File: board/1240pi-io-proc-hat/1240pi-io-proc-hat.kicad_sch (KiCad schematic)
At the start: 6 parts, among them J21 Header, P445 Header, U445 Z80

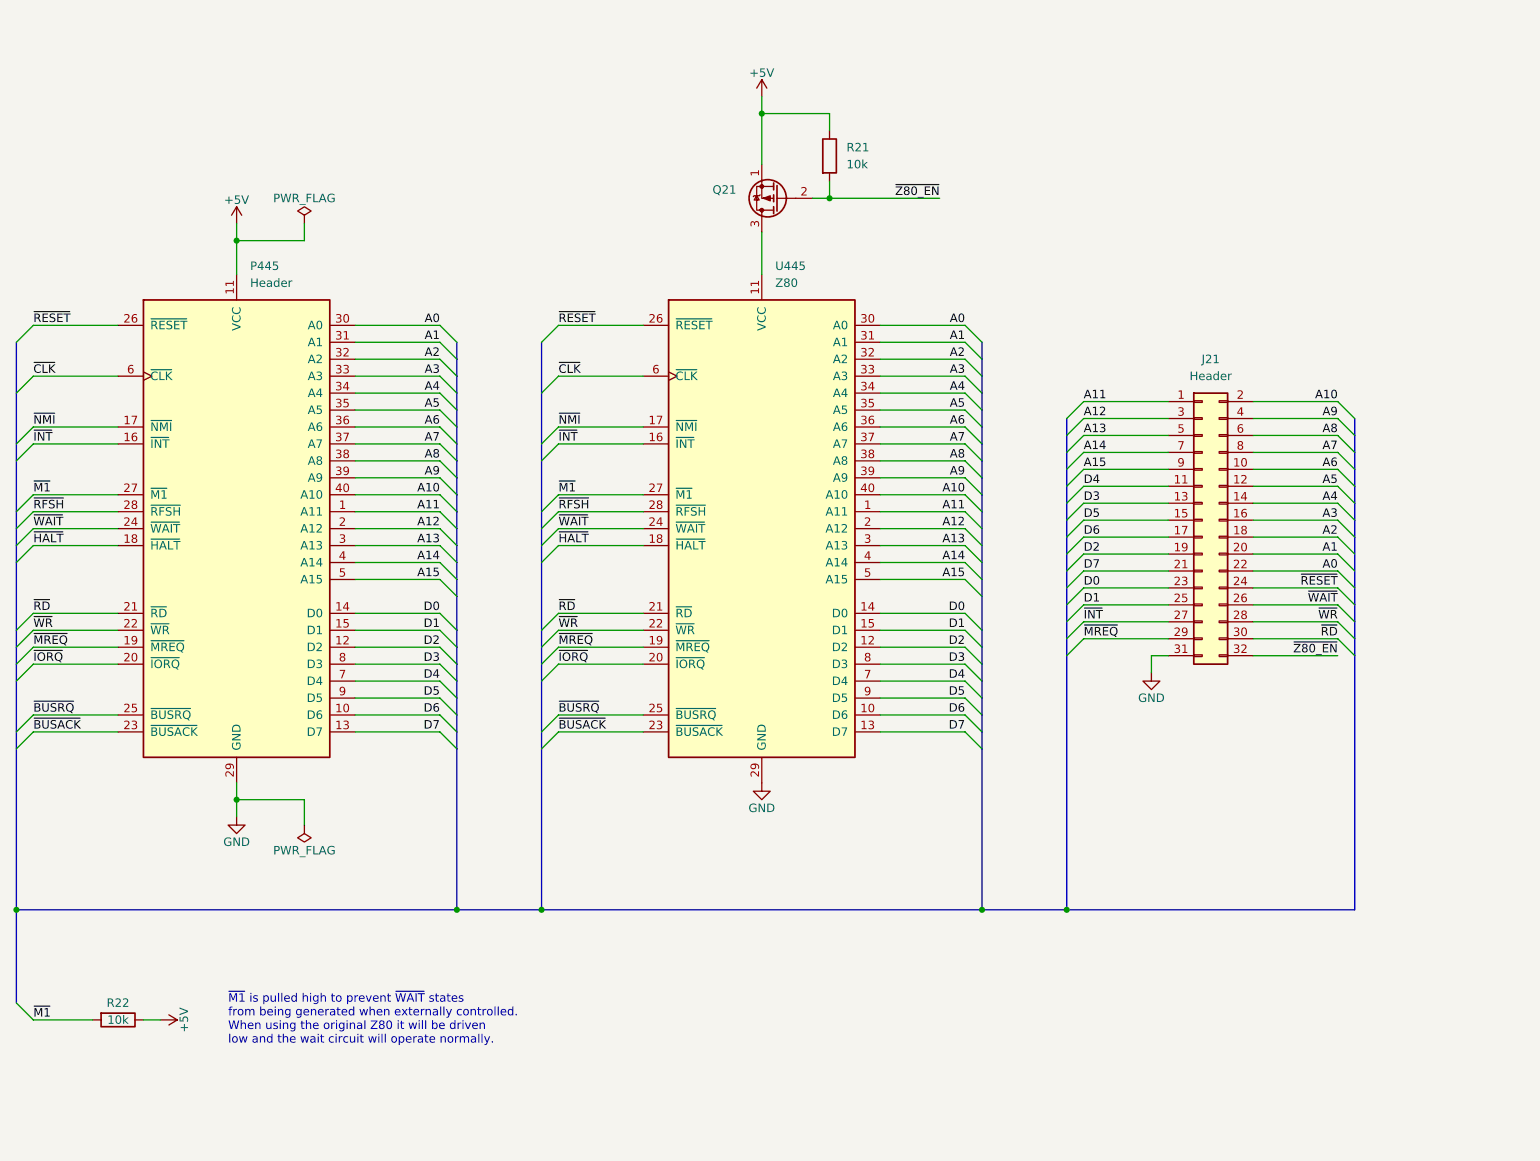
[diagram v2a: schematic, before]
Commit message: Switch hat boards from IDC ribbons to flat flex cables.
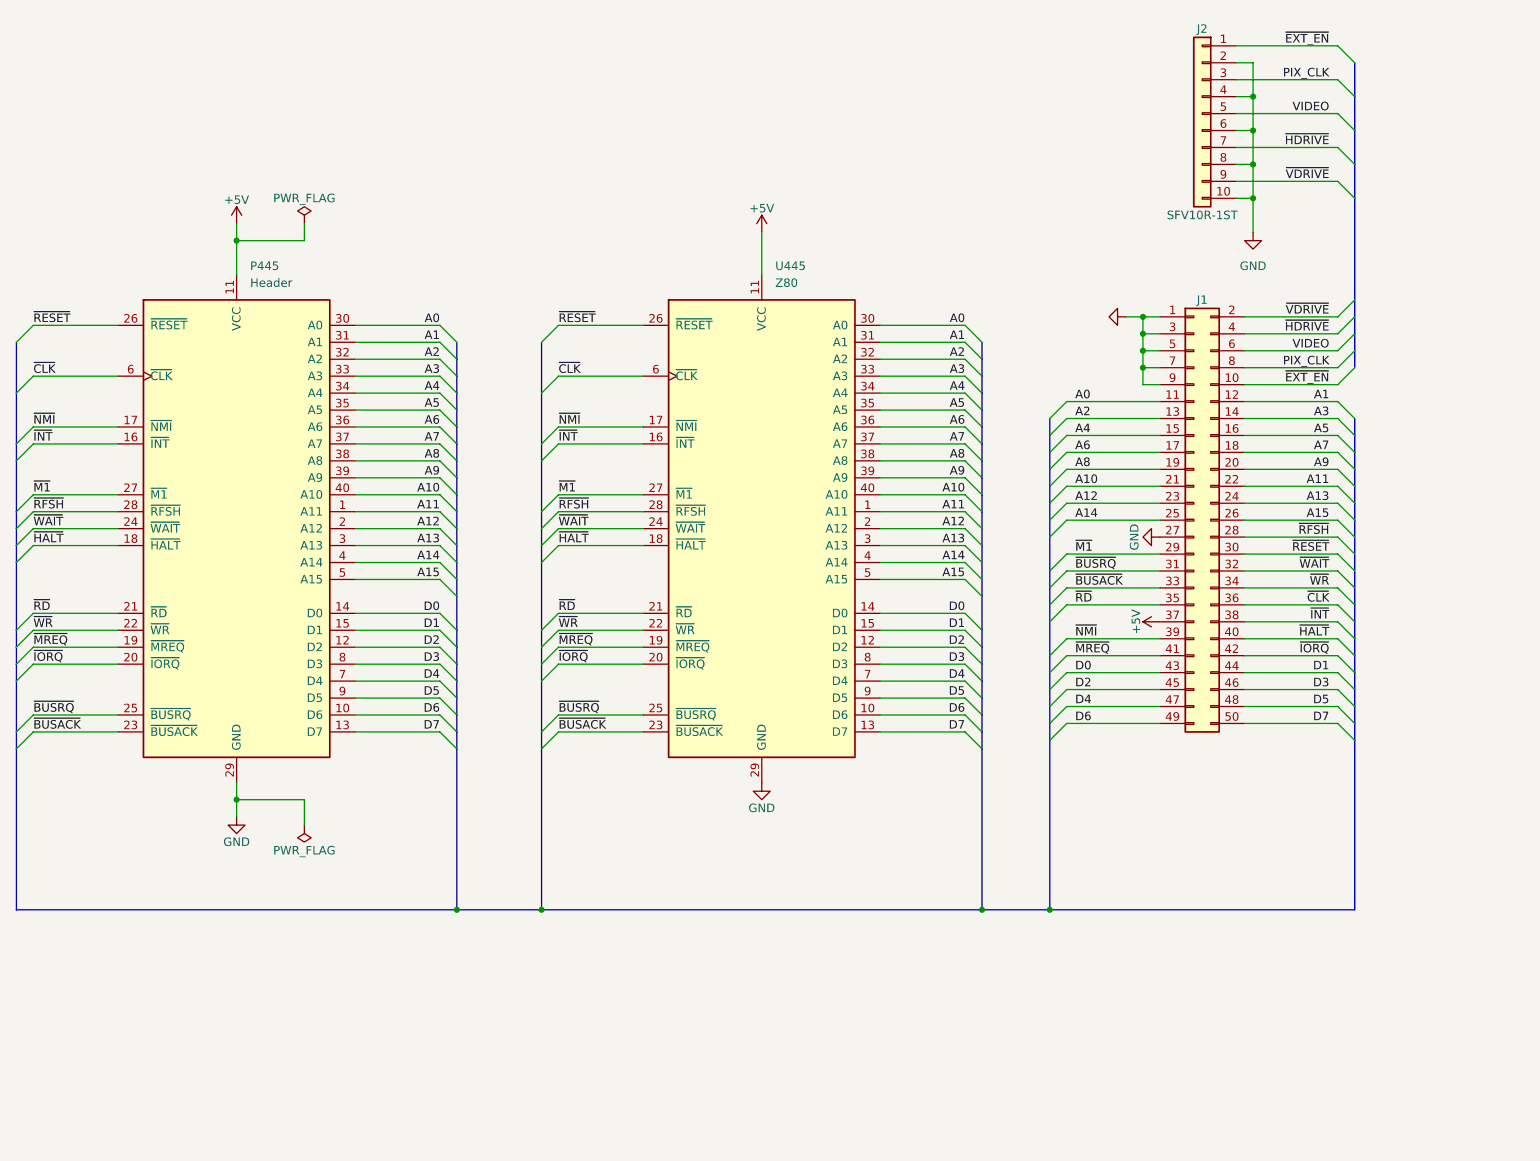
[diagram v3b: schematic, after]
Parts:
- removed J21: Header, Connector_PinHeader_2.54mm:PinHeader_2x16_P2.54mm_Vertical, symbol Connector_Generic:Conn_02x16_Odd_Even
- removed Q21: (no value), Package_TO_SOT_THT:TO-92_Wide, symbol Device:Q_PMOS_SGD
- removed R21, R22: 10k, Resistor_THT:R_Axial_DIN0207_L6.3mm_D2.5mm_P10.16mm_Horizontal, symbol Device:R
- added J1: (no value), symbol Connector_Generic:Conn_02x25_Odd_Even
- added J2: SFV10R-1ST, 0Local:Amphenol_SFV10R-1ST, symbol Connector_Generic:Conn_01x10
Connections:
- net +5V: now also U445.11 (VCC), J1.37 (Pin_37)
- net A0: now also J1.11 (Pin_11)
- net A1: now also J1.12 (Pin_12)
- net A10: now also J1.21 (Pin_21)
- net A11: now also J1.22 (Pin_22)
- net A12: now also J1.23 (Pin_23)
- net A13: now also J1.24 (Pin_24)
- net A14: now also J1.25 (Pin_25)
- net A15: now also J1.26 (Pin_26)
- net A2: now also J1.13 (Pin_13)
- net A3: now also J1.14 (Pin_14)
- net A4: now also J1.15 (Pin_15)
- net A5: now also J1.16 (Pin_16)
- net A6: now also J1.17 (Pin_17)
- net A7: now also J1.18 (Pin_18)
- net A8: now also J1.19 (Pin_19)
- net A9: now also J1.20 (Pin_20)
- net D0: now also J1.43 (Pin_43)
- net D1: now also J1.44 (Pin_44)
- net D2: now also J1.45 (Pin_45)
- net D3: now also J1.46 (Pin_46)
- net D4: now also J1.47 (Pin_47)
- net D5: now also J1.48 (Pin_48)
- net D6: now also J1.49 (Pin_49)
- net D7: now also J1.50 (Pin_50)
- net GND: now also J1.1 (Pin_1), J1.27 (Pin_27), J1.3 (Pin_3), J1.5 (Pin_5), J1.7 (Pin_7), J1.9 (Pin_9), J2.10 (Pin_10), J2.2 (Pin_2), J2.4 (Pin_4), J2.6 (Pin_6), J2.8 (Pin_8)
- net ~{BUSACK}: now also J1.33 (Pin_33)
- net ~{BUSRQ}: now also J1.31 (Pin_31)
- net ~{CLK}: now also J1.36 (Pin_36)
- net ~{HALT}: now also J1.40 (Pin_40)
- net ~{INT}: now also J1.38 (Pin_38)
- net ~{IORQ}: now also J1.42 (Pin_42)
- net ~{M1}: now also J1.29 (Pin_29)
- net ~{MREQ}: now also J1.41 (Pin_41)
- net ~{NMI}: now also J1.39 (Pin_39)
- net ~{RD}: now also J1.35 (Pin_35)
- net ~{RESET}: now also J1.30 (Pin_30)
- net ~{RFSH}: now also J1.28 (Pin_28)
- net ~{WAIT}: now also J1.32 (Pin_32)
- net ~{WR}: now also J1.34 (Pin_34)
- new net PIX_CLK: J1.8 (Pin_8), J2.3 (Pin_3)
- new net VIDEO: J1.6 (Pin_6), J2.5 (Pin_5)
- new net ~{EXT_EN}: J1.10 (Pin_10), J2.1 (Pin_1)
- new net ~{HDRIVE}: J1.4 (Pin_4), J2.7 (Pin_7)
- new net ~{VDRIVE}: J1.2 (Pin_2), J2.9 (Pin_9)
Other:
- note removed: "~{M1} is pulled high to prevent ~{WAIT} states from being generated when externally controlled. When using the original Z80 it will be driven low and the wait circuit will operate normally."
- company: © 2022 Sam Hanes, licensed under CERN-OHL-P v2 -> © 2022 Sam Hanes, licensed under CERN-OHL-S v2

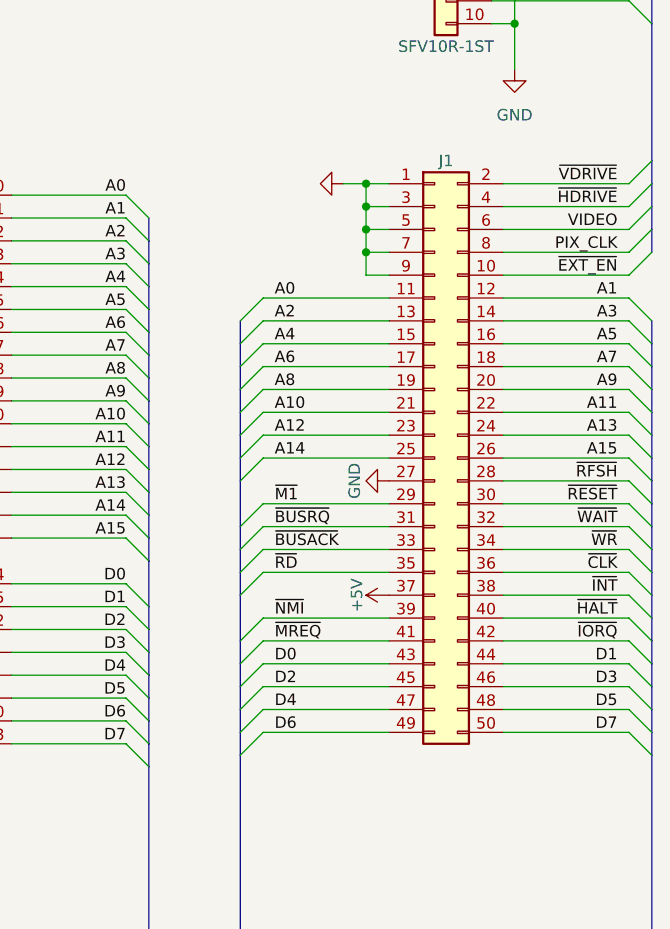
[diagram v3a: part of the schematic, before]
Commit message: Update board license to CERN-OHL-S v2+.
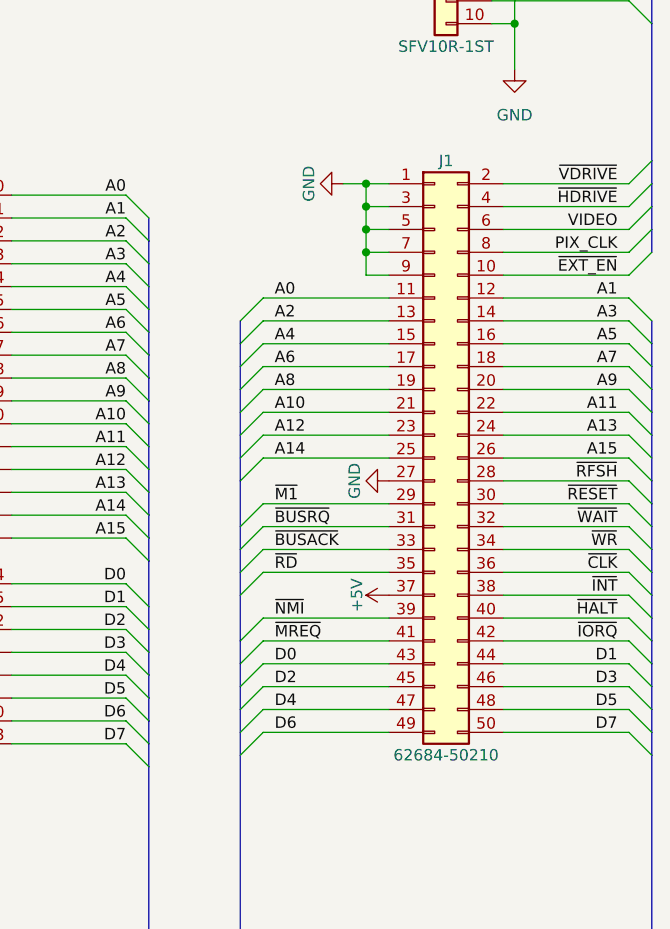
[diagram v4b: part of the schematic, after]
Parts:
- J1: value (none) -> 62684-50210; footprint (none) -> 0Local:Amphenol_62684-50210
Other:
- company: © 2022 Sam Hanes, licensed under CERN-OHL-S v2 -> © 2022 Sam Hanes, licensed under CERN-OHL-S v2+
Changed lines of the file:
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@@
     (date "2022-05-21")
     (rev "1.0")
-    (company "© 2022 Sam Hanes, licensed under CERN-OHL-S v2")
+    (company "© 2022 Sam Hanes, licensed under CERN-OHL-S v2+")
     (comment 1 "https://github.com/Elemecca/1240pi")
   )
@@
     (in_bom yes) (on_board yes)
     (property "Reference" "J1" (id 0) (at 203.2 73.66 0))
-    (property "Value" "" (id 1) (at 203.2 139.7 0))
-    (property "Footprint" "" (id 2) (at 201.93 106.68 0)
+    (property "Value" "62684-50210" (id 1) (at 203.2 139.7 0))
+    (property "Footprint" "0Local:Amphenol_62684-50210" (id 2) (at 201.93 106.68 0)
       (effects (font (size 1.27 1.27)) hide)
     )
@@
       (effects (font (size 1.27 1.27)) hide)
     )
-    (property "Value" "" (id 1) (at 187.96 76.2 0))
+    (property "Value" "GND" (id 1) (at 187.96 76.2 0))
     (property "Footprint" "" (id 2) (at 191.77 76.2 0)
       (effects (font (size 1.27 1.27)) hide)

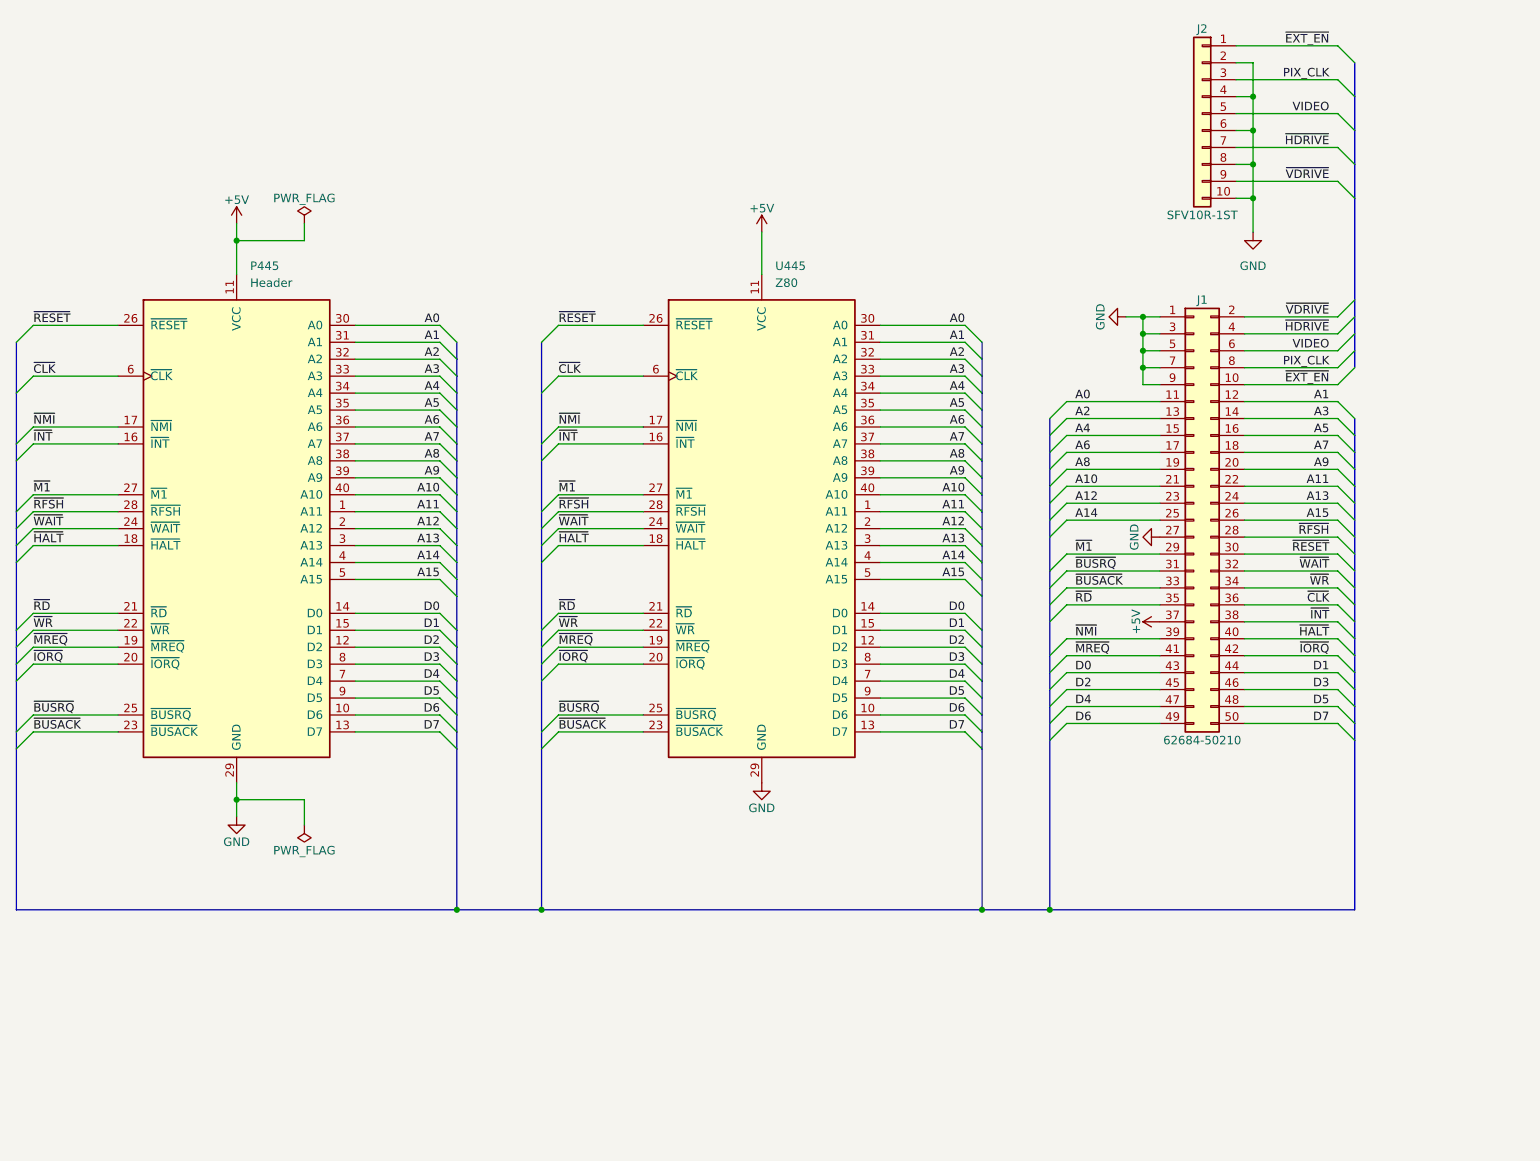
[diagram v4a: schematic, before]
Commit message: Disconnect and pull up Z80 pins not used by the 1240.
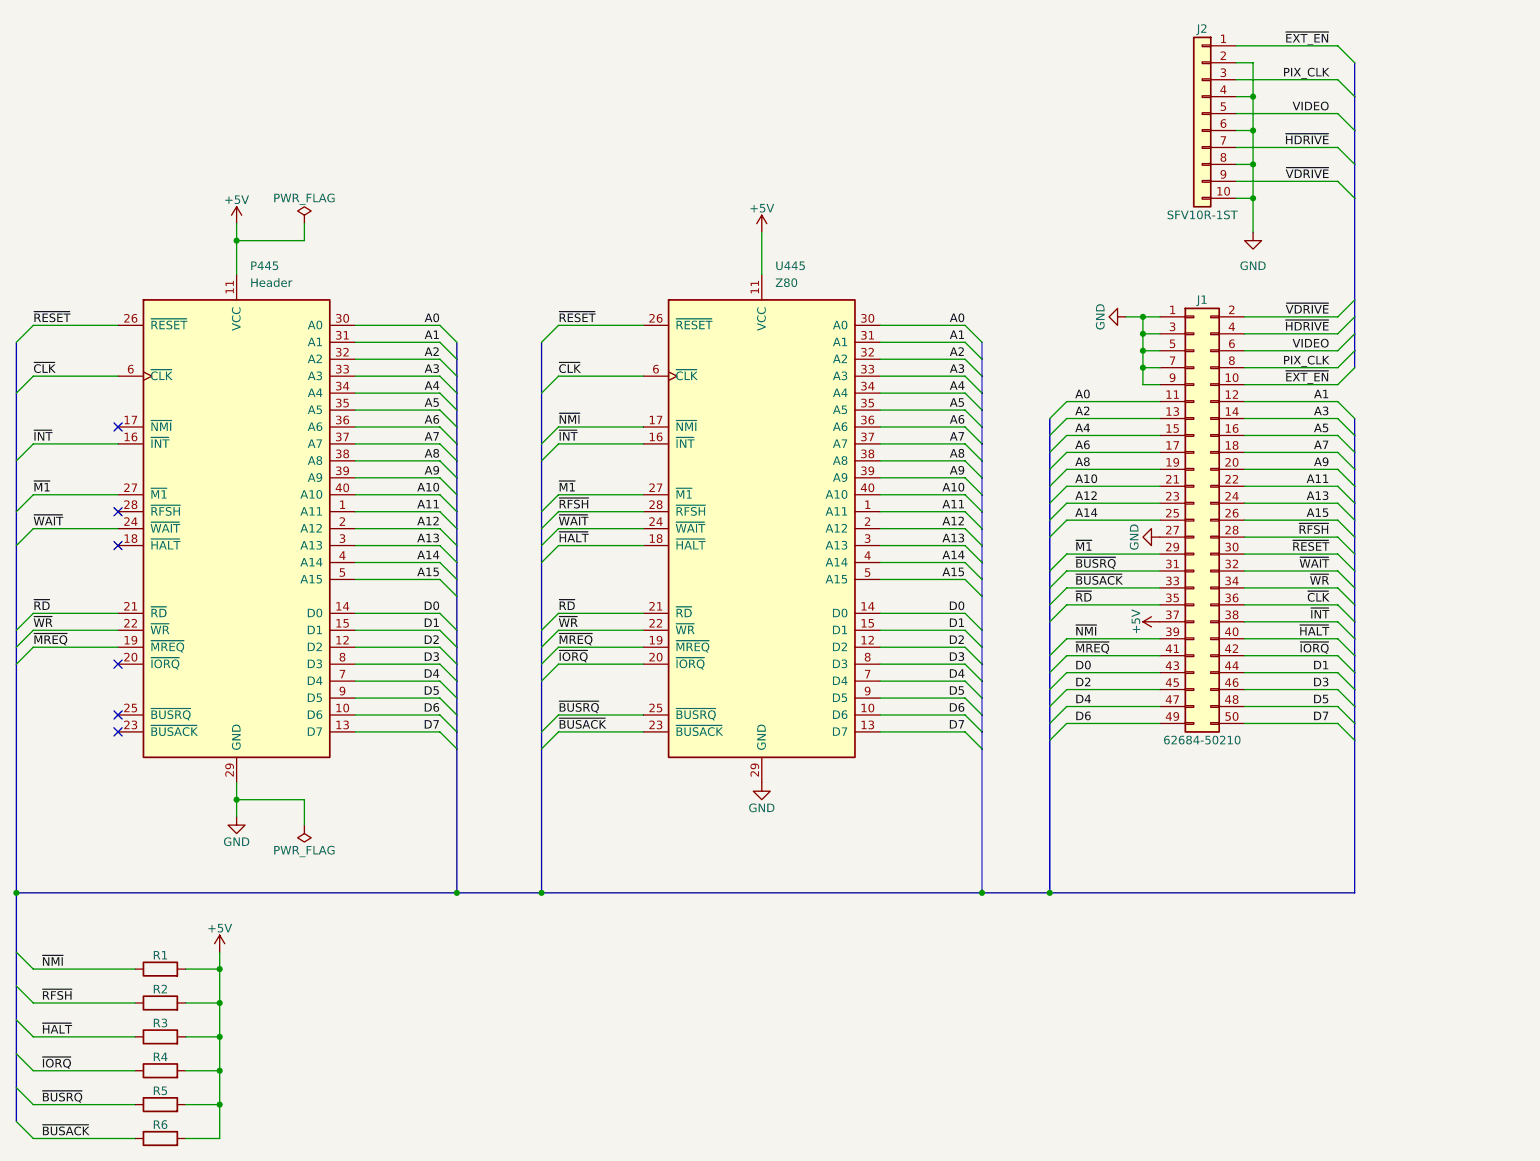
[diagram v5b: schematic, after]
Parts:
- added R1, R2, R3, R4, R5, R6: (no value), symbol Device:R
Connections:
- net +5V: now also R1.2, R2.2, R3.2, R4.2, R5.2, R6.2
- net ~{BUSACK}: now also R6.1; no longer P445.23 (~{BUSACK})
- net ~{BUSRQ}: now also R5.1; no longer P445.25 (~{BUSRQ})
- net ~{HALT}: now also R3.1; no longer P445.18 (~{HALT})
- net ~{IORQ}: now also R4.1; no longer P445.20 (~{IORQ})
- net ~{NMI}: now also R1.1; no longer P445.17 (~{NMI})
- net ~{RFSH}: now also R2.1; no longer P445.28 (~{RFSH})
- no-connect marks 0 -> 6
